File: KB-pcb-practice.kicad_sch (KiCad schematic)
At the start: 21 parts, among them U1 W25Q128JVS, Y1 ABLS-12.000MHZ-B4-T

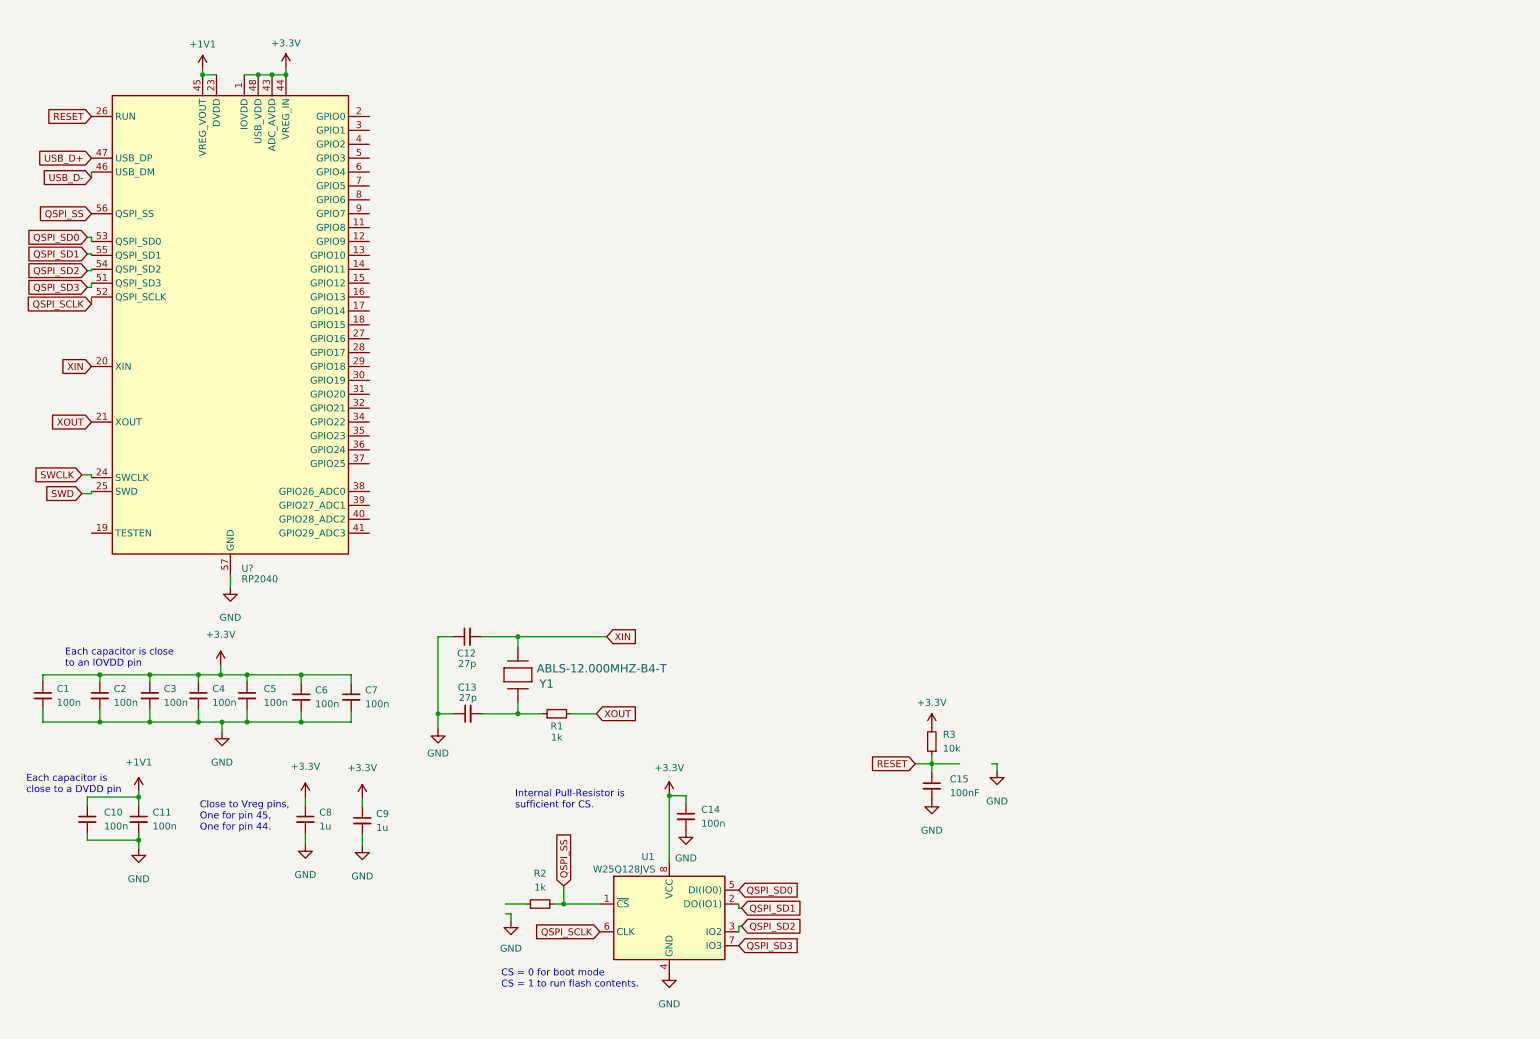
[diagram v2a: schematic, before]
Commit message: Mostly Finished Schematic
Still looking for switches for reset and flash circuit.
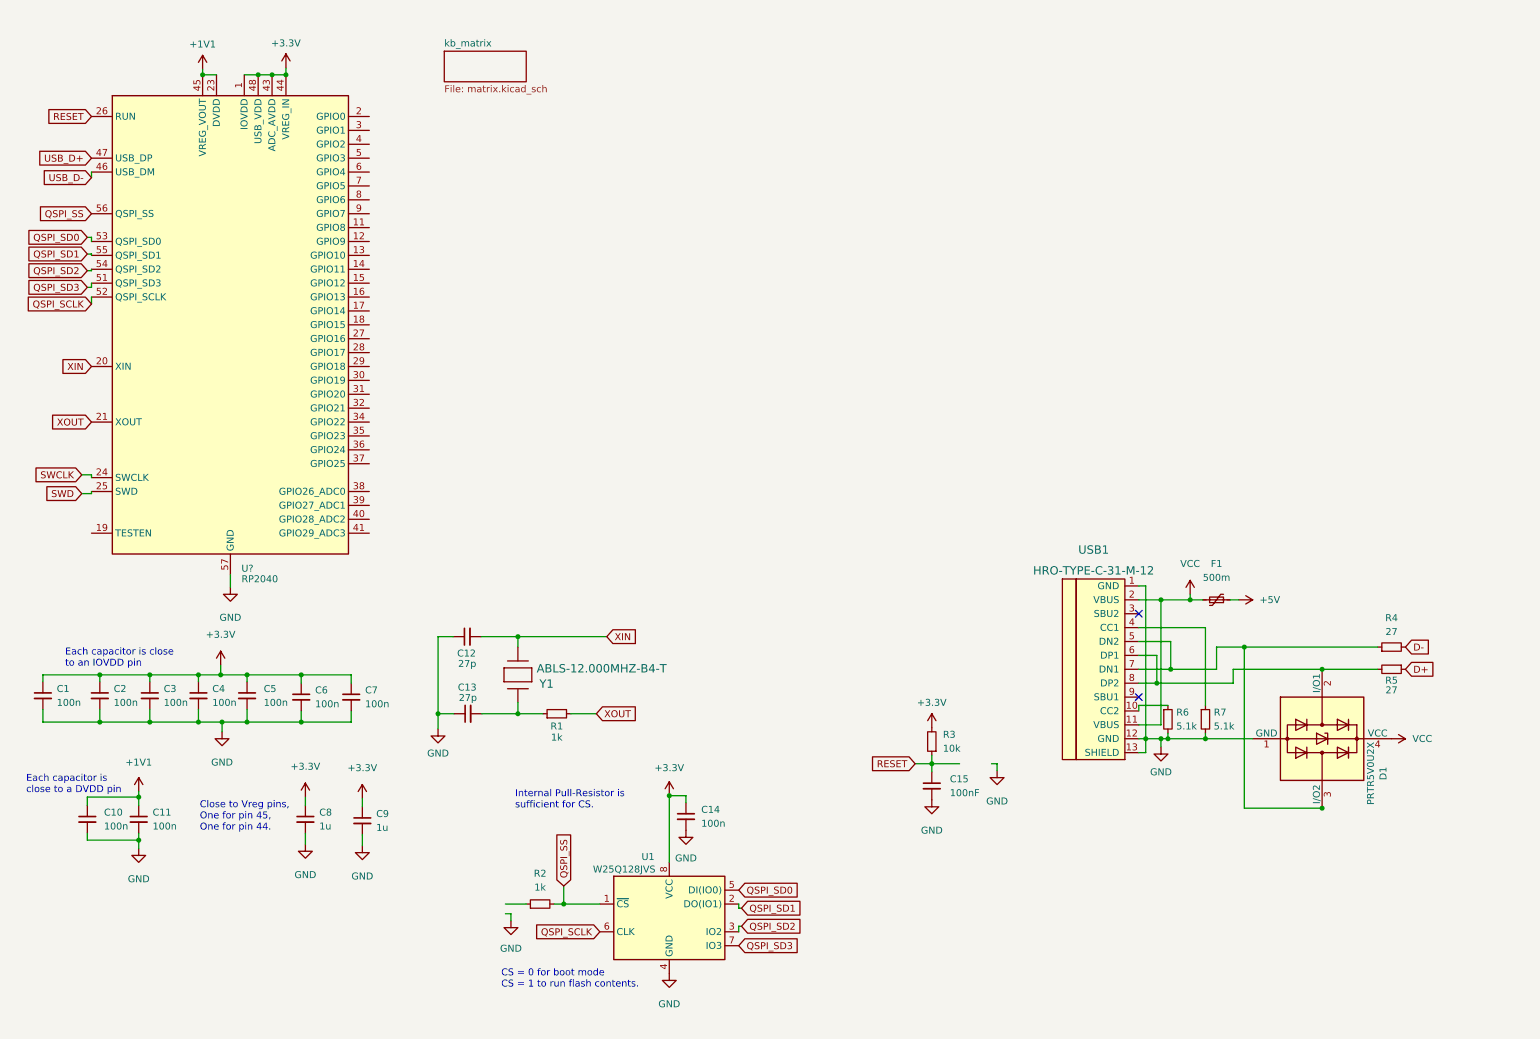
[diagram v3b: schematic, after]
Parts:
- added D1: PRTR5V0U2X, Package_TO_SOT_SMD:SOT-143, symbol Power_Protection:PRTR5V0U2X
- added F1: 500m, symbol Device:Polyfuse_Small
- added R4, R5: 27, symbol Device:R_Small
- added R6, R7: 5.1k, symbol Device:R_Small
- added USB1: HRO-TYPE-C-31-M-12, symbol Type-C:HRO-TYPE-C-31-M-12
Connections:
- net GND: now also D1.1 (GND), R6.2, R7.2, USB1.1 (GND), USB1.12 (GND), USB1.13 (SHIELD)
- new net: R6.1, USB1.10 (CC2)
- new net: R7.1, USB1.4 (CC1)
- new net: D1.3 (I/O2), R4.1, USB1.5 (DN2), USB1.7 (DN1)
- new net: D1.2 (I/O1), R5.2, USB1.6 (DP1), USB1.8 (DP2)
- new net +5V: F1.2
- new net D+: R5.1
- new net D-: R4.2
- new net VCC: D1.4 (VCC), F1.1, USB1.11 (VBUS), USB1.2 (VBUS)
- no-connect marks 0 -> 2
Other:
- added sheet kb_matrix (matrix.kicad_sch)

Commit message: Added SWD circuit, began RGB matrix
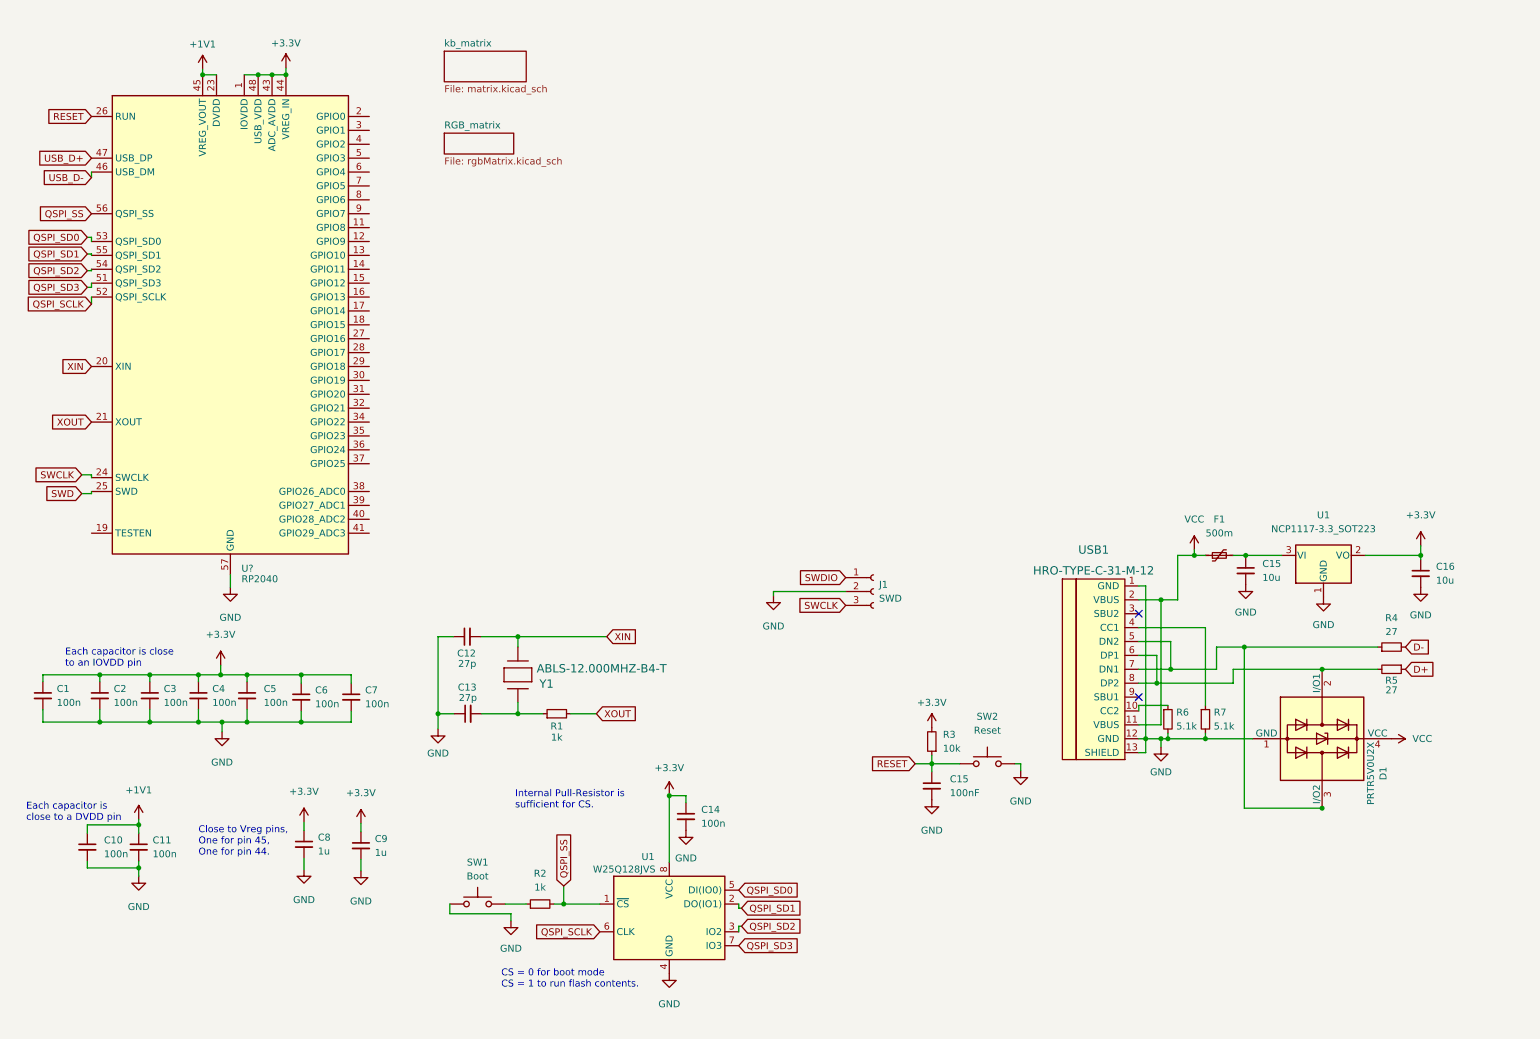
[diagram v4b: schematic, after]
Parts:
- added C15, C16: 10u, symbol Device:C_Small
- added J1: SWD, symbol Connector:Conn_01x03_Female
- added SW1: Boot, symbol Switch:SW_Push
- added SW2: Reset, symbol Switch:SW_Push
- added U1: NCP1117-3.3_SOT223, Package_TO_SOT_SMD:SOT-223-3_TabPin2, symbol Regulator_Linear:NCP1117-3.3_SOT223
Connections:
- net +3.3V: now also C16.1, U1.2 (VO)
- net GND: now also C15.2, C16.2, J1.2 (Pin_2), SW1.1, SW2.2, U1.1 (GND)
- net RESET: now also SW2.1
- net SWCLK: now also J1.3 (Pin_3)
- net at R2.1: now also SW1.2
- net +5V: no longer names the net of F1.2
- net +5V: now also C15.1, U1.3 (VI)
- new net SWDIO: J1.1 (Pin_1)
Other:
- added sheet RGB_matrix (rgbMatrix.kicad_sch)
- moved on the sheet: C10, C11, C8, C9, F1

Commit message: Started work on Led sch,
Decided on led driver IC
Decided on led part
started work on led matrix
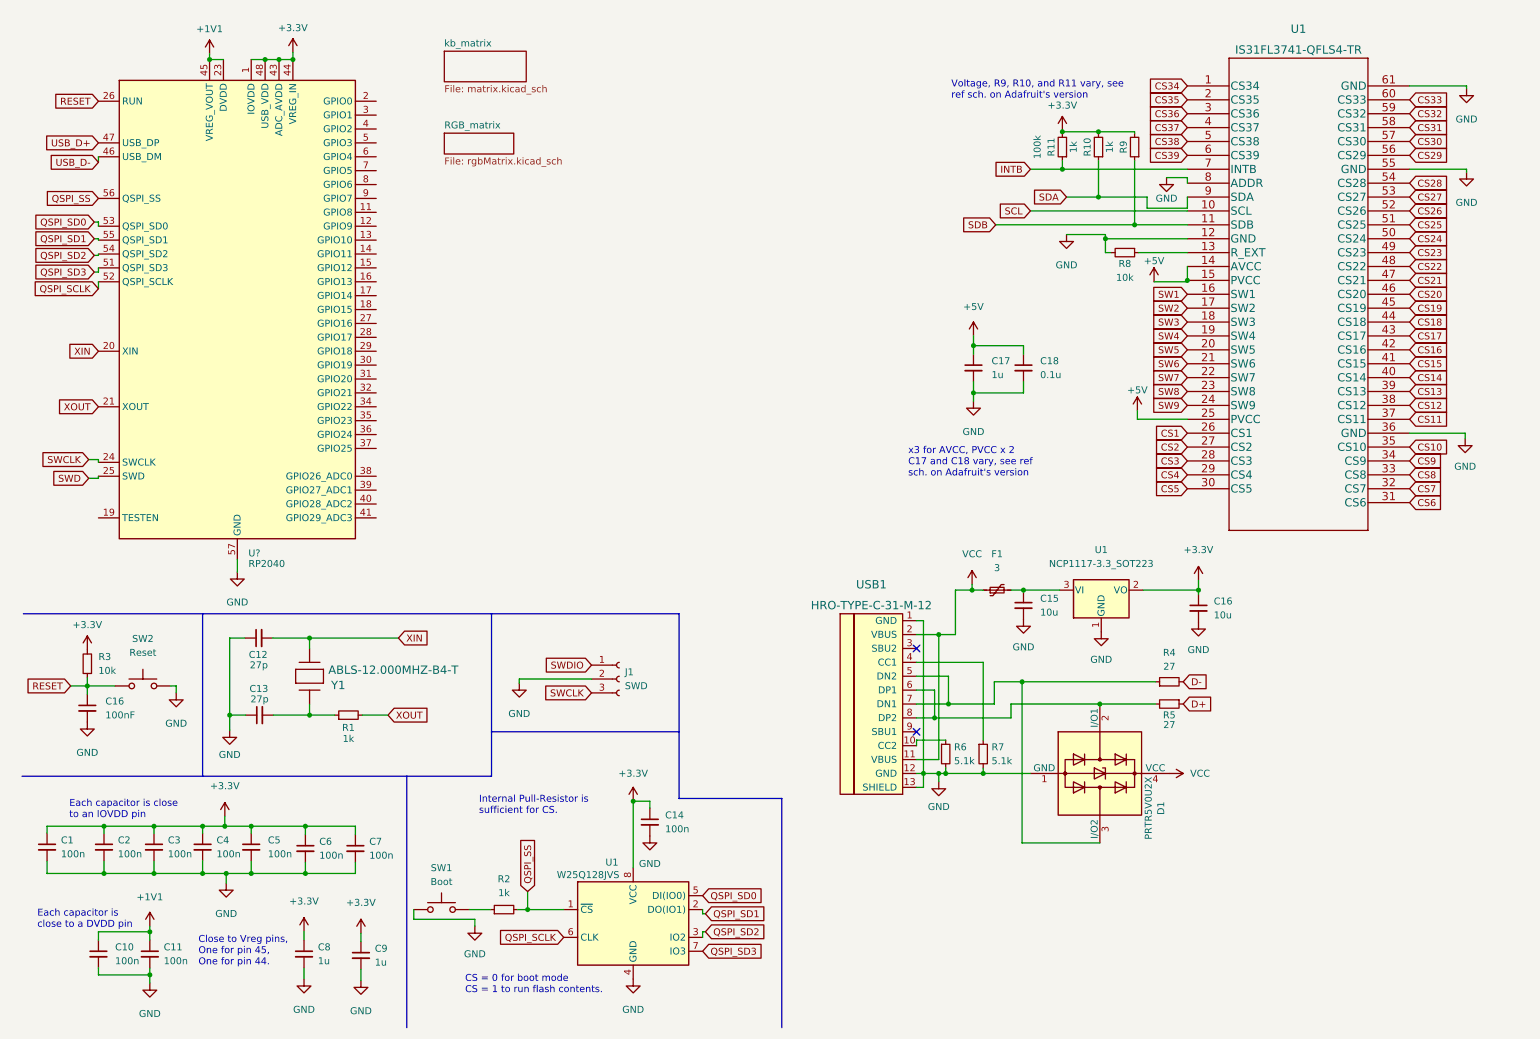
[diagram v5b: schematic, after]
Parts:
- added C17: 1u, symbol Device:C_Small
- added C18: 0.1u, symbol Device:C_Small
- added R10, R9: 1k, symbol Device:R_Small
- added R11: 100k, symbol Device:R_Small
- added R8: 10k, symbol Device:R_Small
- added U1: IS31FL3741-QFLS4-TR, QFN60_ISI, symbol ul_IS31FL3741-QFLS4-TR:IS31FL3741-QFLS4-TR
- F1: value 500m -> 3
- renumbered C15 to C16
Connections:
- net +3.3V: now also R10.2, R11.2, R9.2
- net GND: now also C17.2, C18.2, R8.2, U1.12 (GND), U1.36 (GND), U1.55 (GND), U1.61 (GND), U1.8 (ADDR)
- new net: R8.1, U1.13 (R_EXT)
- new net +5V: C17.1, C18.1, U1.14 (AVCC), U1.15 (PVCC), U1.25 (PVCC)
- new net CS1: U1.26 (CS1)
- new net CS10: U1.35 (CS10)
- new net CS11: U1.37 (CS11)
- new net CS12: U1.38 (CS12)
- new net CS13: U1.39 (CS13)
- new net CS14: U1.40 (CS14)
- new net CS15: U1.41 (CS15)
- new net CS16: U1.42 (CS16)
- new net CS17: U1.43 (CS17)
- new net CS18: U1.44 (CS18)
- new net CS19: U1.45 (CS19)
- new net CS2: U1.27 (CS2)
- new net CS20: U1.46 (CS20)
- new net CS21: U1.47 (CS21)
- new net CS22: U1.48 (CS22)
- new net CS23: U1.49 (CS23)
- new net CS24: U1.50 (CS24)
- new net CS25: U1.51 (CS25)
- new net CS26: U1.52 (CS26)
- new net CS27: U1.53 (CS27)
- new net CS28: U1.54 (CS28)
- new net CS29: U1.56 (CS29)
- new net CS3: U1.28 (CS3)
- new net CS30: U1.57 (CS30)
- new net CS31: U1.58 (CS31)
- new net CS32: U1.59 (CS32)
- new net CS33: U1.60 (CS33)
- new net CS34: U1.1 (CS34)
- new net CS35: U1.2 (CS35)
- new net CS36: U1.3 (CS36)
- new net CS37: U1.4 (CS37)
- new net CS38: U1.5 (CS38)
- new net CS39: U1.6 (CS39)
- new net CS4: U1.29 (CS4)
- new net CS5: U1.30 (CS5)
- new net CS6: U1.31 (CS6)
- new net CS7: U1.32 (CS7)
- new net CS8: U1.33 (CS8)
- new net CS9: U1.34 (CS9)
- new net INTB: R11.1, U1.7 (INTB)
- new net SCL: U1.10 (SCL)
- new net SDA: R10.1, U1.9 (SDA)
- new net SDB: R9.1, U1.11 (SDB)
- new net SW1: U1.16 (SW1)
- new net SW2: U1.17 (SW2)
- new net SW3: U1.18 (SW3)
- new net SW4: U1.19 (SW4)
- new net SW5: U1.20 (SW5)
- new net SW6: U1.21 (SW6)
- new net SW7: U1.22 (SW7)
- new net SW8: U1.23 (SW8)
- new net SW9: U1.24 (SW9)
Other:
- note added: "Voltage, R9, R10, and R11 vary, see ref sch. on Adafruit's version"
- note added: "x3 for AVCC, PVCC x 2 C17 and C18 vary, see ref sch. on Adafruit's version"
- moved on the sheet: C1, C10, C11, C12, C13, C14, C15, C16, C2, C3, C4, C5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

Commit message: Changed led driver
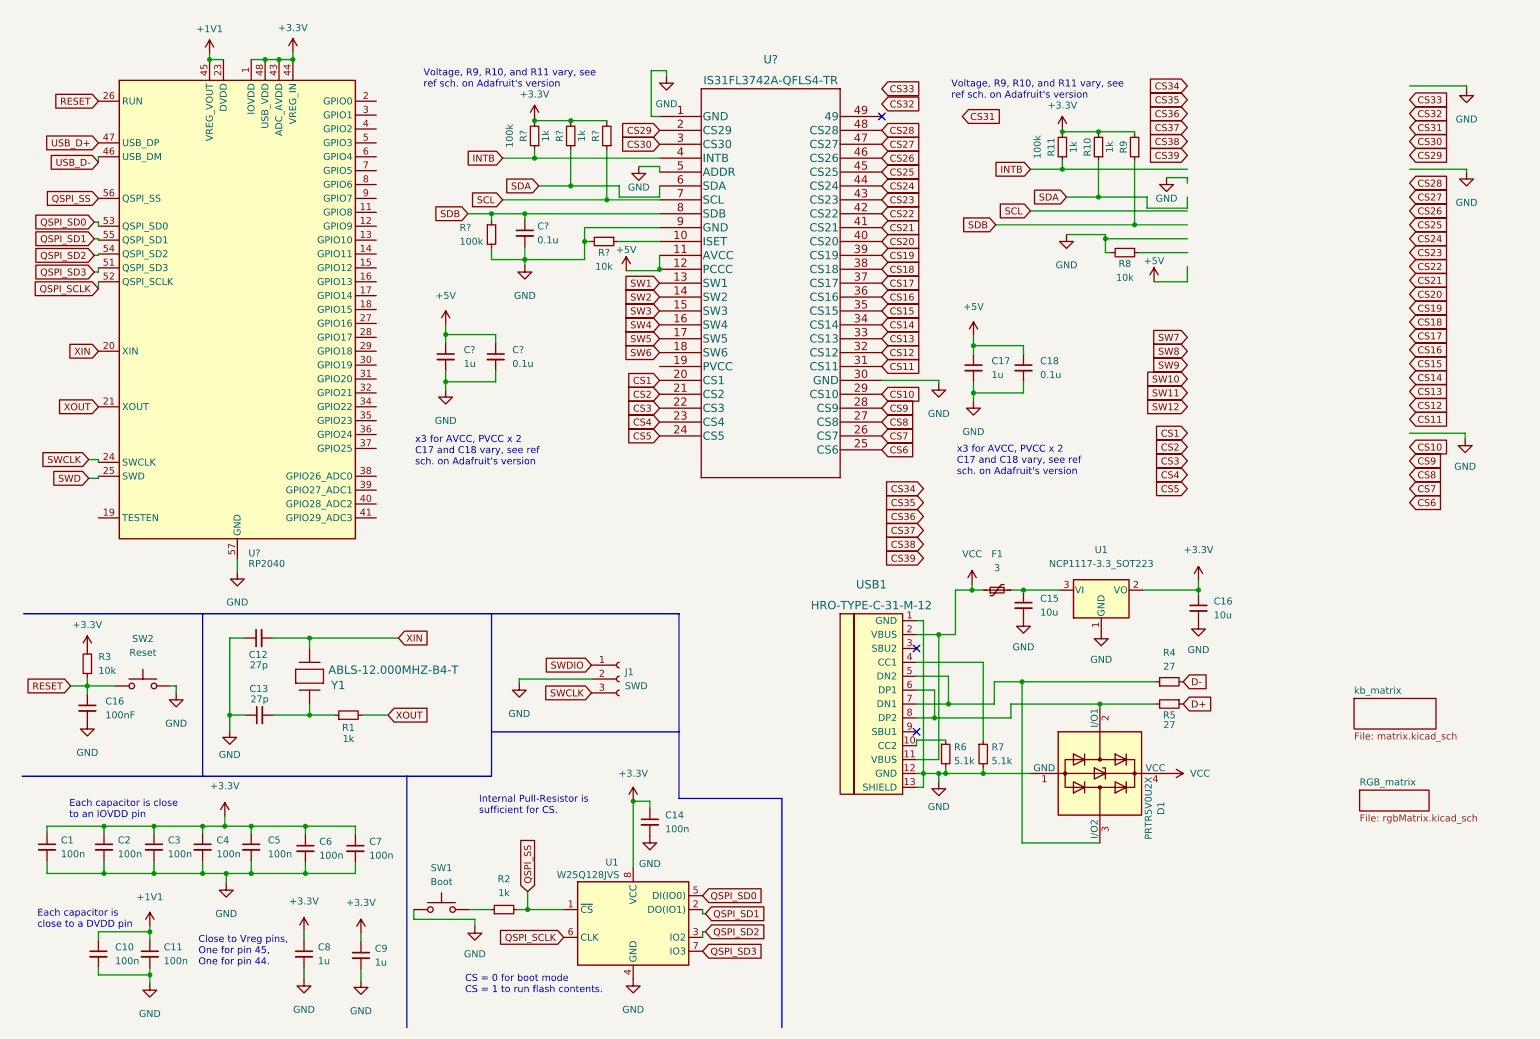
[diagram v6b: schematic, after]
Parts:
- removed U1: IS31FL3741-QFLS4-TR, QFN60_ISI, symbol ul_IS31FL3741-QFLS4-TR:IS31FL3741-QFLS4-TR
- added C?: 1u, symbol Device:C_Small
- added C? (x2): 0.1u, symbol Device:C_Small
- added R? (x2): 100k, symbol Device:R_Small
- added R? (x2): 1k, symbol Device:R_Small
- added R?: 10k, symbol Device:R_Small
- added U?: IS31FL3742A-QFLS4-TR, QFN48_IS31FL3742A-QFLS4-TR_ISI, symbol ul_IS31FL3742A-QFLS4-TR:IS31FL3742A-QFLS4-TR
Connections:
- net +3.3V: now also R?.2, R?.2, R?.2
- net +5V: now also C?.1, C?.1, U?.11 (AVCC), U?.12 (PCCC)
- net CS1: now also U?.20 (CS1)
- net CS10: now also U?.29 (CS10)
- net CS11: now also U?.31 (CS11)
- net CS12: now also U?.32 (CS12)
- net CS13: now also U?.33 (CS13)
- net CS14: now also U?.34 (CS14)
- net CS15: now also U?.35 (CS15)
- net CS16: now also U?.36 (CS16)
- net CS17: now also U?.37 (CS17)
- net CS18: now also U?.38 (CS18)
- net CS19: now also U?.39 (CS19)
- net CS2: now also U?.21 (CS2)
- net CS20: now also U?.40 (CS20)
- net CS21: now also U?.41 (CS21)
- net CS22: now also U?.42 (CS22)
- net CS23: now also U?.43 (CS23)
- net CS24: now also U?.44 (CS24)
- net CS25: now also U?.45 (CS25)
- net CS26: now also U?.46 (CS26)
- net CS27: now also U?.47 (CS27)
- net CS28: now also U?.48 (CS28)
- net CS29: now also U?.2 (CS29)
- net CS3: now also U?.22 (CS3)
- net CS30: now also U?.3 (CS30)
- net CS4: now also U?.23 (CS4)
- net CS5: now also U?.24 (CS5)
- net CS6: now also U?.25 (CS6)
- net CS7: now also U?.26 (CS7)
- net CS8: now also U?.27 (CS8)
- net CS9: now also U?.28 (CS9)
- net GND: now also C?.2, C?.2, C?.2, R?.2, R?.2, U?.1 (GND), U?.30 (GND), U?.5 (ADDR), U?.9 (GND)
- net INTB: now also R?.1, U?.4 (INTB)
- net SCL: now also R?.1, U?.7 (SCL)
- net SDA: now also R?.1, U?.6 (SDA)
- net SDB: now also C?.1, R?.1, U?.8 (SDB)
- net SW1: now also U?.13 (SW1)
- net SW2: now also U?.14 (SW2)
- net SW3: now also U?.15 (SW3)
- net SW4: now also U?.16 (SW4)
- net SW5: now also U?.17 (SW5)
- net SW6: now also U?.18 (SW6)
- new net: R?.1, U?.10 (ISET)
- no-connect marks 2 -> 3
